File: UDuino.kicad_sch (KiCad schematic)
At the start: 23 parts, among them J101 Barrel_Jack, J102 Conn_01x02_Female, J103 PMOD1, J104 Conn_01x03_Male, J105 Conn_01x03_Male, J106 Conn_01x04_Male, J107 Conn_01x04_Male, U101 STM32F072VBTx

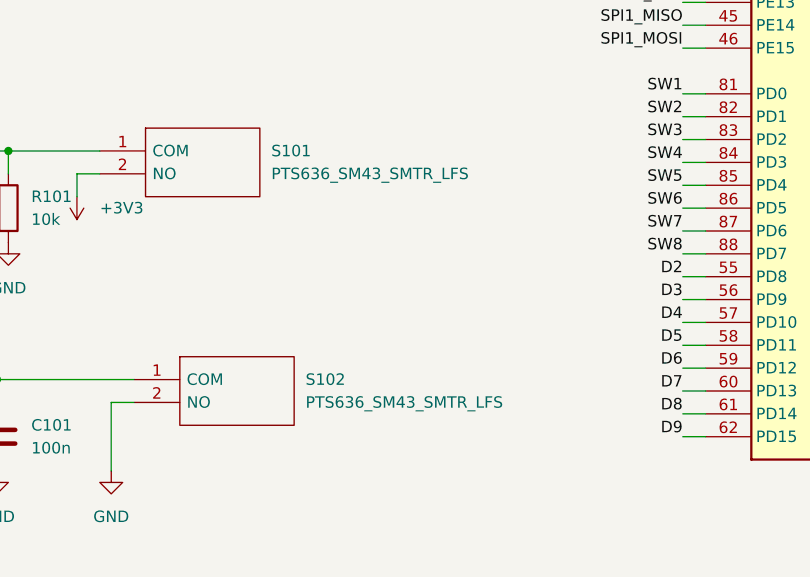
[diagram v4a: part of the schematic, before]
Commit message: Fixed BOM and Silkscreen things
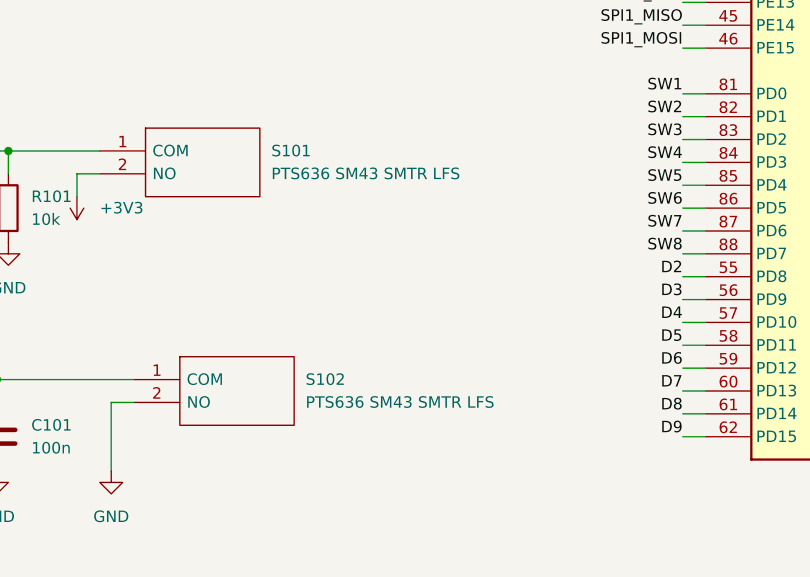
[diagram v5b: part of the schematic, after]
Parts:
- S101, S102: value PTS636_SM43_SMTR_LFS -> PTS636 SM43 SMTR LFS
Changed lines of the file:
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@@
       (effects (font (size 1.27 1.27)) (justify left))
     )
-    (property "Value" "PTS636_SM43_SMTR_LFS" (id 1) (at 58.42 134.6199 0)
+    (property "Value" "PTS636 SM43 SMTR LFS" (id 1) (at 58.42 134.6199 0)
       (effects (font (size 1.27 1.27)) (justify left))
     )
@@
       (effects (font (size 1.27 1.27)) (justify left))
     )
-    (property "Value" "PTS636_SM43_SMTR_LFS" (id 1) (at 62.23 160.0199 0)
+    (property "Value" "PTS636 SM43 SMTR LFS" (id 1) (at 62.23 160.0199 0)
       (effects (font (size 1.27 1.27)) (justify left))
     )
@@
     )
     (path "/0b8a300d-cb05-4f08-95a6-62c312199468/f72b8d5d-c1ec-434d-946e-9833e6ce0896"
-      (reference "P1401") (unit 1) (value "USB_C_Plug") (footprint "Connector_USB:USB_C_Receptacle_Palconn_UTC16-G")
+      (reference "P1401") (unit 1) (value "USB4105-GF-A") (footprint "Connector_USB:USB_C_Receptacle_Palconn_UTC16-G")
     )
     (path "/74114fa7-3930-46b1-8d47-2b12a2f25cb0/a3c26ba8-ef7e-4a30-abe2-d3286603d2cc"
@@
     )
     (path "/426d3cfd-42d6-4600-b624-6c5b46037cf9"
-      (reference "S101") (unit 1) (value "PTS636_SM43_SMTR_LFS") (footprint "PTS636SM43SMTRLFS")
+      (reference "S101") (unit 1) (value "PTS636 SM43 SMTR LFS") (footprint "PTS636SM43SMTRLFS")
     )
     (path "/ff45ee6e-ca17-4876-b21a-fa98aeb33420"
-      (reference "S102") (unit 1) (value "PTS636_SM43_SMTR_LFS") (footprint "PTS636SM43SMTRLFS")
+      (reference "S102") (unit 1) (value "PTS636 SM43 SMTR LFS") (footprint "PTS636SM43SMTRLFS")
     )
     (path "/789c7c0c-b213-4b21-a8c6-519557a78601/3b492ba7-fefe-4ac7-abed-7e2ef82dee46"
@@
     )
     (path "/ec0f2664-2bbf-448f-addb-bf6ed0854f7f/96a58eed-825b-4f44-9c9c-466c94c2861a"
-      (reference "S1001") (unit 1) (value "PTS636_SM43_SMTR_LFS") (footprint "Custom:PTS636SM43SMTRLFS")
+      (reference "S1001") (unit 1) (value "PTS636 SM43 SMTR LFS") (footprint "PTS636SM43SMTRLFS")
     )
     (path "/ec0f2664-2bbf-448f-addb-bf6ed0854f7f/c77c7a10-7562-47af-a401-a49fe2dddd12"
-      (reference "S1002") (unit 1) (value "PTS636_SM43_SMTR_LFS") (footprint "PTS636SM43SMTRLFS")
+      (reference "S1002") (unit 1) (value "PTS636 SM43 SMTR LFS") (footprint "PTS636SM43SMTRLFS")
     )
     (path "/ec0f2664-2bbf-448f-addb-bf6ed0854f7f/fb5206d6-0dc6-4f3b-b464-7d90f8c7ac35"
-      (reference "S1003") (unit 1) (value "PTS636_SM43_SMTR_LFS") (footprint "PTS636SM43SMTRLFS")
+      (reference "S1003") (unit 1) (value "PTS636 SM43 SMTR LFS") (footprint "PTS636SM43SMTRLFS")
     )
     (path "/ec0f2664-2bbf-448f-addb-bf6ed0854f7f/9e1a719b-230c-4f4e-90d3-c3b30fb05c66"
-      (reference "S1004") (unit 1) (value "PTS636_SM43_SMTR_LFS") (footprint "PTS636SM43SMTRLFS")
+      (reference "S1004") (unit 1) (value "PTS636 SM43 SMTR LFS") (footprint "PTS636SM43SMTRLFS")
     )
     (path "/ec0f2664-2bbf-448f-addb-bf6ed0854f7f/0383183f-546e-46ed-83d9-da8bd5caaf4f"
-      (reference "S1005") (unit 1) (value "PTS636_SM43_SMTR_LFS") (footprint "PTS636SM43SMTRLFS")
+      (reference "S1005") (unit 1) (value "PTS636 SM43 SMTR LFS") (footprint "PTS636SM43SMTRLFS")
     )
     (path "/f342b15e-991f-4399-a302-377e00e18460"

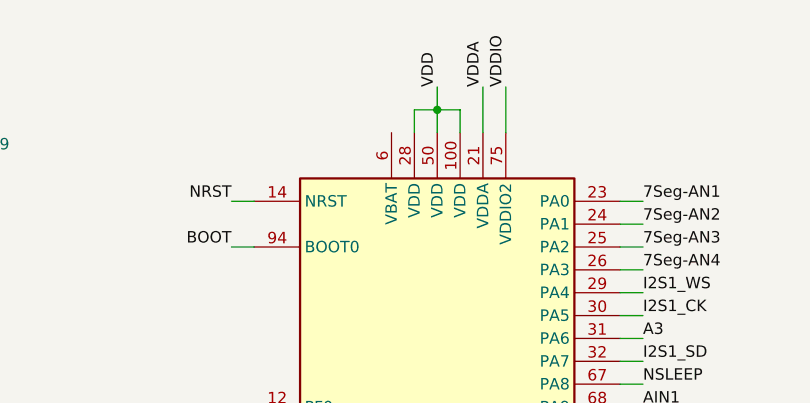
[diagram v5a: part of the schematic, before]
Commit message: Fixed 7seg display
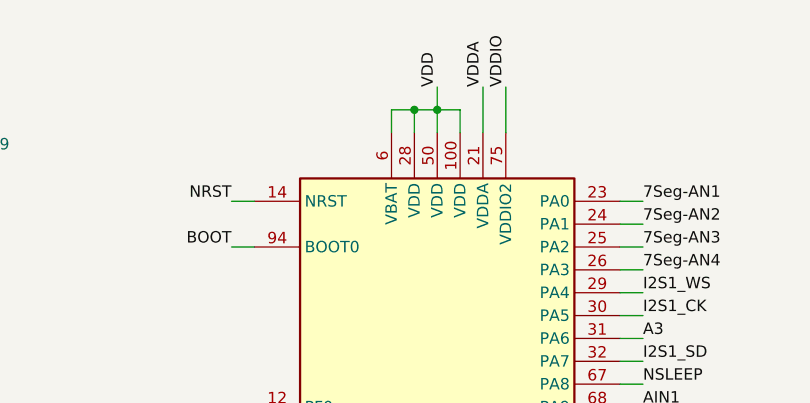
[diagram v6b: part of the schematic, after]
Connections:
- net +3V3: now also U101.6 (VBAT)
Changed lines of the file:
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@@
   (junction (at 219.71 203.2) (diameter 0) (color 0 0 0 0)
   )
+  (junction (at 124.46 29.21) (diameter 0) (color 0 0 0 0)
+  )
   (junction (at 48.26 27.94) (diameter 0) (color 0 0 0 0)
   )
@@
     (stroke (width 0) (type default) (color 0 0 0 0))
   )
+  (wire (pts (xy 121.92 29.21) (xy 124.46 29.21))
+    (stroke (width 0) (type default) (color 0 0 0 0))
+  )
   (wire (pts (xy 320.04 121.92) (xy 322.58 121.92))
     (stroke (width 0) (type default) (color 0 0 0 0))
@@
     (stroke (width 0) (type default) (color 0 0 0 0))
   )
+  (wire (pts (xy 121.92 31.75) (xy 121.92 29.21))
+    (stroke (width 0) (type default) (color 0 0 0 0))
+  )
   (wire (pts (xy 260.35 52.07) (xy 260.35 33.02))
     (stroke (width 0) (type default) (color 0 0 0 0))
@@
       (reference "#PWR0139") (unit 1) (value "+3V3") (footprint "")
     )
+    (path "/74114fa7-3930-46b1-8d47-2b12a2f25cb0/540b62a6-2c94-4339-b20b-ca29ce7c2f63"
+      (reference "#PWR0140") (unit 1) (value "+3V3") (footprint "")
+    )
+    (path "/74114fa7-3930-46b1-8d47-2b12a2f25cb0/10b8cc7e-fcc9-4cbd-80d0-2540882d50f0"
+      (reference "#PWR0141") (unit 1) (value "+3V3") (footprint "")
+    )
+    (path "/74114fa7-3930-46b1-8d47-2b12a2f25cb0/5f48c77e-d134-43ed-b383-82844d03c5d4"
+      (reference "#PWR0142") (unit 1) (value "+3V3") (footprint "")
+    )
+    (path "/74114fa7-3930-46b1-8d47-2b12a2f25cb0/92ba47c5-34bf-4d8b-adfa-0b93671073ea"
+      (reference "#PWR0143") (unit 1) (value "+3V3") (footprint "")
+    )
     (path "/1c23098d-f383-4116-8a8d-5e1d3a0dd8e6/3fb587e6-f7fd-4042-b289-9e9a38ddf5bc"
       (reference "#PWR0201") (unit 1) (value "+3V3") (footprint "")
@@
       (reference "#PWR0801") (unit 1) (value "GND") (footprint "")
     )
-    (path "/74114fa7-3930-46b1-8d47-2b12a2f25cb0/93f1ffb4-9ed2-4b22-9dbf-05f1364a963c"
-      (reference "#PWR0901") (unit 1) (value "+5V") (footprint "")
-    )
-    (path "/74114fa7-3930-46b1-8d47-2b12a2f25cb0/a832dbd2-e5ce-4bc0-8fb3-1893be54df22"
-      (reference "#PWR0902") (unit 1) (value "+5V") (footprint "")
-    )
-    (path "/74114fa7-3930-46b1-8d47-2b12a2f25cb0/1d614869-8701-4f11-8e4a-9cec58a505a9"
-      (reference "#PWR0903") (unit 1) (value "+5V") (footprint "")
-    )
-    (path "/74114fa7-3930-46b1-8d47-2b12a2f25cb0/769be495-2ac2-4c03-8d83-4d3471df4c67"
-      (reference "#PWR0904") (unit 1) (value "+5V") (footprint "")
-    )
     (path "/ec0f2664-2bbf-448f-addb-bf6ed0854f7f/0a6a2c8e-a3c9-4d9f-b4a9-ffceba275409"
       (reference "#PWR01001") (unit 1) (value "+3V3") (footprint "")
@@
     )
     (path "/74114fa7-3930-46b1-8d47-2b12a2f25cb0/d89df24a-e3cd-4a2c-95d9-43e0416acbc4"
-      (reference "R905") (unit 1) (value "220") (footprint "Resistor_SMD:R_0603_1608Metric")
+      (reference "R905") (unit 1) (value "147") (footprint "Resistor_SMD:R_0603_1608Metric")
     )
     (path "/74114fa7-3930-46b1-8d47-2b12a2f25cb0/a2c421f4-3f33-469b-a9a4-72392462350e"
-      (reference "R906") (unit 1) (value "220") (footprint "Resistor_SMD:R_0603_1608Metric")
+      (reference "R906") (unit 1) (value "147") (footprint "Resistor_SMD:R_0603_1608Metric")
     )
     (path "/74114fa7-3930-46b1-8d47-2b12a2f25cb0/5fc9b9bc-e11c-4d9f-8980-b6b6497bd56d"
-      (reference "R907") (unit 1) (value "220") (footprint "Resistor_SMD:R_0603_1608Metric")
+      (reference "R907") (unit 1) (value "147") (footprint "Resistor_SMD:R_0603_1608Metric")
     )
     (path "/74114fa7-3930-46b1-8d47-2b12a2f25cb0/dabe150f-1f0e-429f-bc11-bf8cbd9b184b"
-      (reference "R908") (unit 1) (value "220") (footprint "Resistor_SMD:R_0603_1608Metric")
+      (reference "R908") (unit 1) (value "147") (footprint "Resistor_SMD:R_0603_1608Metric")
     )
     (path "/74114fa7-3930-46b1-8d47-2b12a2f25cb0/e3366da8-3a1c-4630-b259-e5d9e89cf6c6"
-      (reference "R909") (unit 1) (value "220") (footprint "Resistor_SMD:R_0603_1608Metric")
+      (reference "R909") (unit 1) (value "147") (footprint "Resistor_SMD:R_0603_1608Metric")
     )
     (path "/74114fa7-3930-46b1-8d47-2b12a2f25cb0/d2eec7b0-b42d-4557-8588-05bcf7c666a2"
-      (reference "R910") (unit 1) (value "220") (footprint "Resistor_SMD:R_0603_1608Metric")
+      (reference "R910") (unit 1) (value "147") (footprint "Resistor_SMD:R_0603_1608Metric")
     )
     (path "/74114fa7-3930-46b1-8d47-2b12a2f25cb0/25e899e6-a3f8-4f7b-92d5-dbbdae80d990"
-      (reference "R911") (unit 1) (value "220") (footprint "Resistor_SMD:R_0603_1608Metric")
+      (reference "R911") (unit 1) (value "147") (footprint "Resistor_SMD:R_0603_1608Metric")
     )
     (path "/74114fa7-3930-46b1-8d47-2b12a2f25cb0/18c15f85-ea16-4a2a-ae15-7d93f70ec2c1"
-      (reference "R912") (unit 1) (value "220") (footprint "Resistor_SMD:R_0603_1608Metric")
+      (reference "R912") (unit 1) (value "147") (footprint "Resistor_SMD:R_0603_1608Metric")
     )
     (path "/ec0f2664-2bbf-448f-addb-bf6ed0854f7f/70b30843-a72c-4f51-82e5-fba26f6bd1b3"
